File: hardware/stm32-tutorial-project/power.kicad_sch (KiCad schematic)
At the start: 16 parts, among them J1 USB_C_Receptacle_USB2.0_14P, U2 AZ1117-3.3

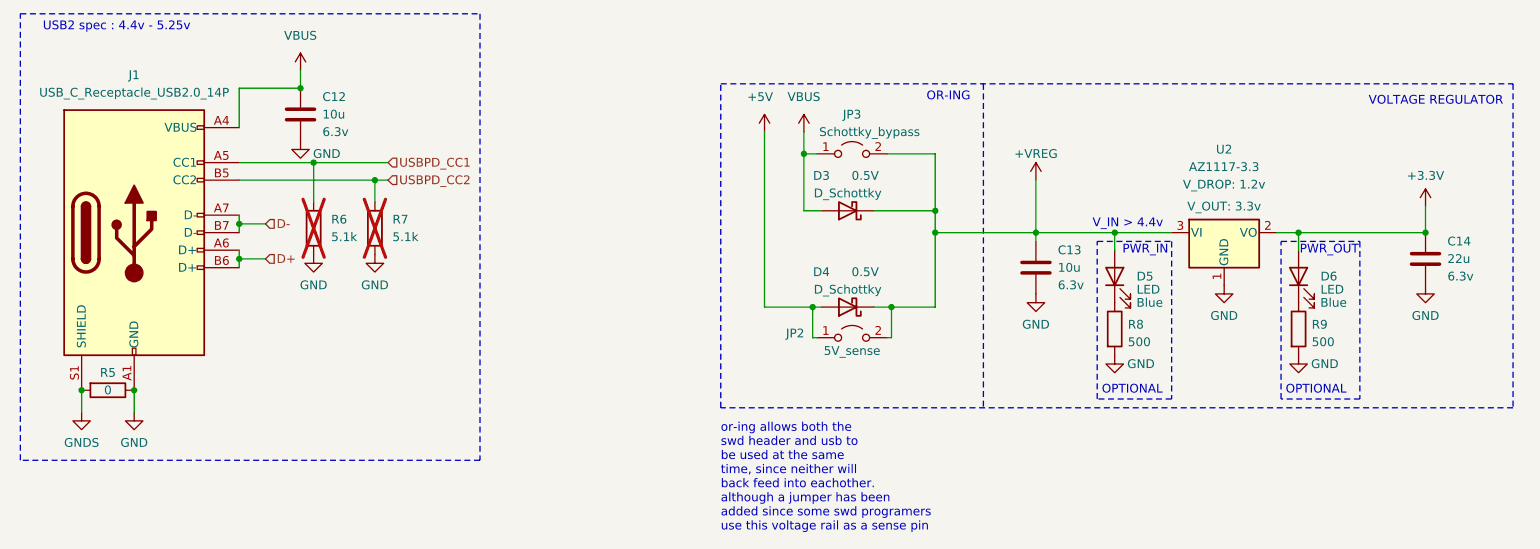
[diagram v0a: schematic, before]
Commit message: added esd diodes
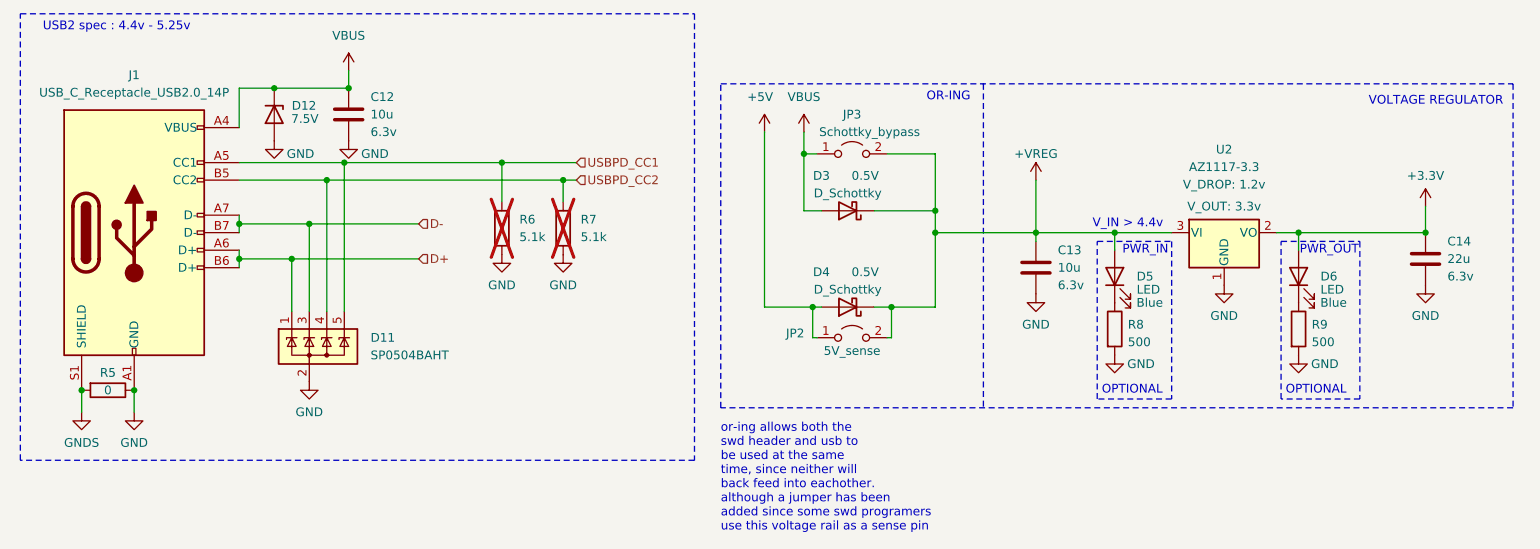
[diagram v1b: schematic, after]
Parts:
- added D11: SP0504BAHT, Package_TO_SOT_SMD:SOT-23-5, symbol Power_Protection:SP0504BAHT
- added D12: PTVS7V5Z1USK, Diode_SMD:Nexperia_DSN1608-2_1.6x0.8mm, symbol Diode:PTVS7V5Z1USK
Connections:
- net D+: now also D11.1 (K)
- net D-: now also D11.3 (K)
- net GND: now also D11.2 (A), D12.2 (A)
- net USBPD_CC1: now also D11.5 (K)
- net USBPD_CC2: now also D11.4 (K)
- net VBUS: now also D12.1 (K)
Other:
- moved on the sheet: C12, R6, R7
